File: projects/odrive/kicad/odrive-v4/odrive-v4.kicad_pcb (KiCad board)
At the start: 4 copper layers, 170 x 115 mm, 378 parts, among them J1 PC 16/2-ST, J10 ENC_M1_JST-GH, J11 ENC_SPI_JST-GH, J12 GPIO_2x4, J13 BRAKE_EXT, J2 M0 A/B/C, J3 M1 A/B/C, J4 FTSH-105-01-L-DV-K, J5 FAN 12V 150mA MAX, J6 USB4105-GF-A, J7 JST-GH-4 CAN, J8 JST-GH-4 CAN, J9 ENC_M0_JST-GH, Q1 NVMFS5C628NL | BSC027N10NS5, Q10 NVMFS5C628NL, Q11 NVMFS5C628NL, Q12 NVMFS5C628NL, Q13 NVMFS5C628NL, Q14 NVMFS5C628NL, Q15 NVMFS5C628NL, Q16 NVMFS5C628NL, Q17 NVMFS5C628NL, Q18 NVMFS5C628NL, Q19 NVMFS5C628NL, Q20 NVMFS5C628NL, Q21 NVMFS5C628NL, Q30 NVMFS5C628NL, Q31 NVMFS5C628NL, Q32 NVMFS5C628NL, Q33 NVMFS5C628NL, Q34 NVMFS5C628NL, Q35 NVMFS5C628NL, Q36 NVMFS5C628NL, Q37 NVMFS5C628NL, Q38 NVMFS5C628NL, Q39 NVMFS5C628NL, Q40 NVMFS5C628NL, Q41 NVMFS5C628NL, Q50 NVMFS5C628NL/BSC027N10NS5, Q51 NVMFS5C628NL/BSC027N10NS5, SW1 CAN_TERM, U10 TLV9062, U11 TMUX1204, U12 TLV7031, U13 TLV431, U14 74LVC1G04, U15 74LVC1G08, U16 TPD4E05U06, U2 STM32F405RGT6, U20 LM5164DDA, U21 LMR51430, U22 TLV75533PDBV, U23 TPS7A2033DBV, U25 74LVC1G06, U26 TLV7031DBV, U27 74LVC1G08, U28 TPS3840DL30, U3 DRV8353RS, U30 TPS2553DBV, U31 TPS2553DBV, U32 TPS2553DBV, U33 USBLC6-2SC6, U34 TCAN1042HGV, U35 SN74LVC2G17, U36 SN74LVC2G17, U37 SN74LVC2G17, U38 TPD4E05U06, U39 TPD4E05U06, U4 DRV8353RS, U40 SN74LVC1G125, U41 TPD4E05U06, U42 TPD1E10B06, U50 UCC27517A, U51 INA181A2, U52 TLV7031, U53 74LVC1G74, U54 74LVC1G32, U55 74LVC1G08, Y1 8MHz

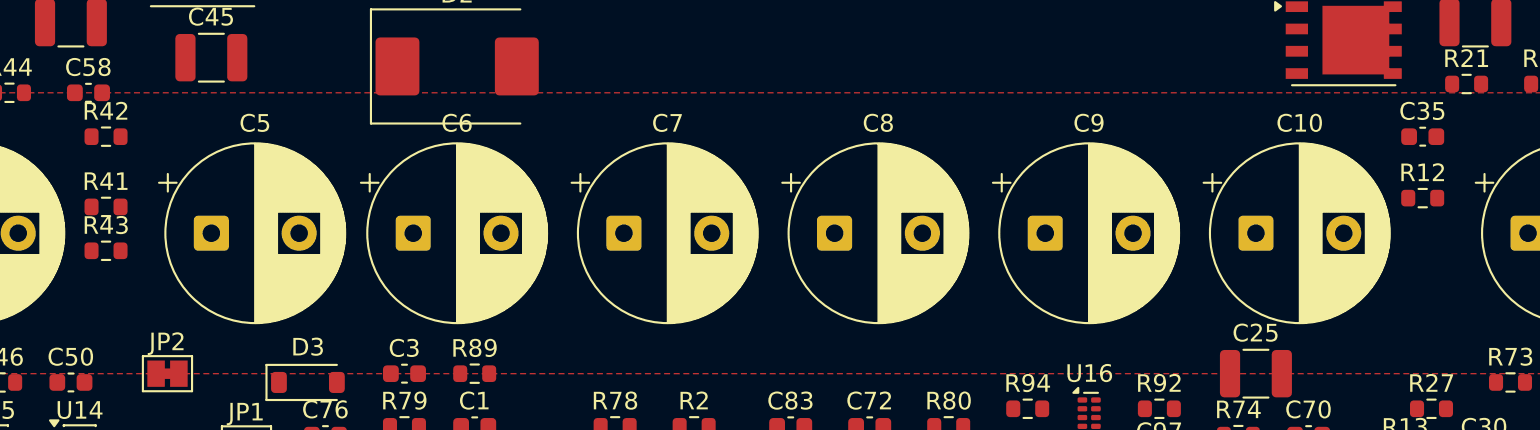
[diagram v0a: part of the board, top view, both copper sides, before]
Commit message: Even out the bulk bank pitch, and add M3 mounting holes to the schematic
The bank was on one line but not evenly spaced - the gaps ran 16, 11.5, 12,
12, 12, 12, 15.5 mm, because the earlier pass snapped Y to a row and kept
whatever X the shelf packer had left. Visibly uneven once you zoom in. Now a
uniform 13 mm pitch from 87 to 178, which leaves 3 mm of air between the 10 mm
bodies. Verdict stays pass with no hard failures.

Also keeps H1-H4: plated M3 mounting holes belong in the schematic so the pads
land on GND in the netlist rather than showing up as stray copper. ERC is still
clean at 0 violations. They are not pushed to the board yet - that needs an
update_pcb_from_schematic run.
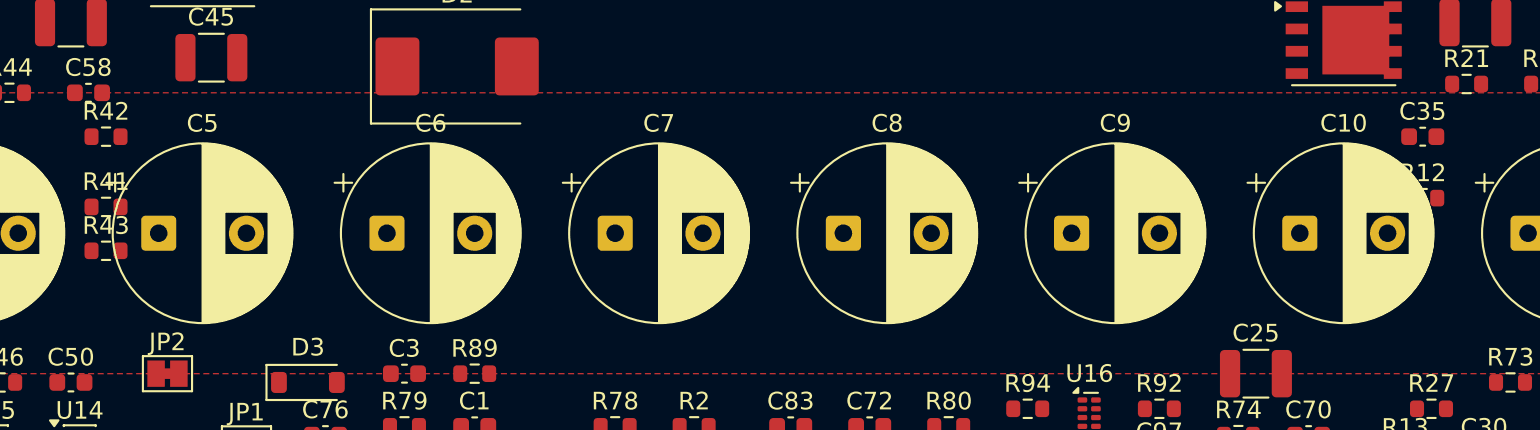
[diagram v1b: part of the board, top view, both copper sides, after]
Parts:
- moved C5 3.00 mm to (100.0, 100.0)
- moved C10 2.50 mm to (165.0, 100.0)
- moved C6 1.50 mm to (113.0, 100.0)
- moved C9 1.50 mm to (152.0, 100.0)
- moved C7 0.50 mm to (126.0, 100.0)
- moved C8 0.50 mm to (139.0, 100.0)
